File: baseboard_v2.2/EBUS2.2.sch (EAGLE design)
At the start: 51 parts, among them IC1 TLC393P, IC2 78L05Z

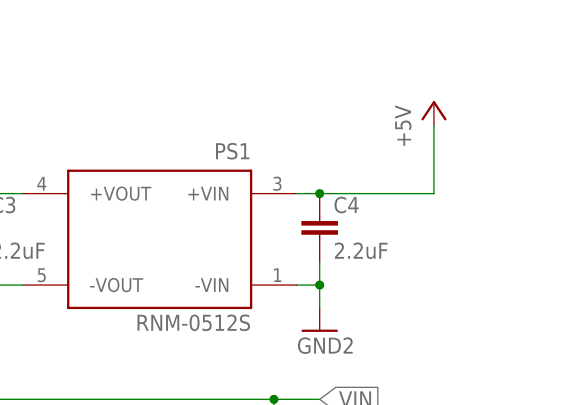
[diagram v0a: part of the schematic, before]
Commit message: change external power pinout
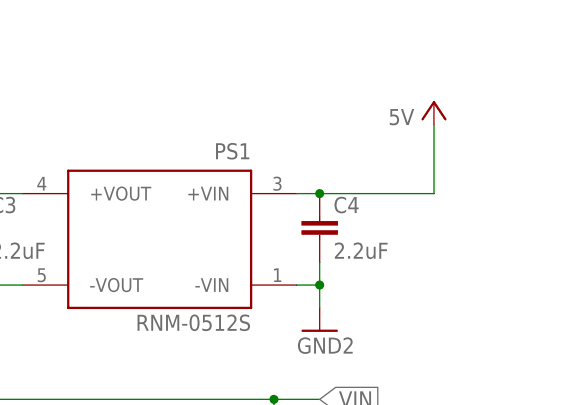
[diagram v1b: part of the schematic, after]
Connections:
- net +5V: no longer C4.1, PS1.+VIN
- net 5V: now also C4.1, PS1.+VIN
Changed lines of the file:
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@@
 <layer number="91" name="Nets" color="2" fill="1" visible="yes" active="yes"/>
 <layer number="92" name="Busses" color="1" fill="1" visible="yes" active="yes"/>
-<layer number="93" name="Pins" color="2" fill="1" visible="no" active="yes"/>
+<layer number="93" name="Pins" color="2" fill="1" visible="yes" active="yes"/>
 <layer number="94" name="Symbols" color="4" fill="1" visible="yes" active="yes"/>
 <layer number="95" name="Names" color="7" fill="1" visible="yes" active="yes"/>
@@
 <attribute name="VALUE" x="291.084" y="180.721" size="1.778" layer="96" font="vector"/>
 </instance>
-<instance part="P+7" gate="1" x="302.26" y="198.12" smashed="yes">
-<attribute name="VALUE" x="299.72" y="193.04" size="1.778" layer="96" rot="R90"/>
-</instance>
+<instance part="P+7" gate="1" x="302.26" y="198.12" smashed="yes"/>
 <instance part="GND15" gate="1" x="289.56" y="172.72" smashed="yes">
 <attribute name="VALUE" x="287.02" y="170.18" size="1.778" layer="96"/>
@@
 <wire x1="76.2" y1="71.12" x2="88.9" y2="71.12" width="0.1524" layer="91"/>
 <label x="88.9" y="71.12" size="1.778" layer="95" xref="yes"/>
+</segment>
+<segment>
+<pinref part="P+7" gate="1" pin="+5V"/>
+<wire x1="302.26" y1="195.58" x2="302.26" y2="187.96" width="0.1524" layer="91"/>
+<pinref part="PS1" gate="G$1" pin="+VIN"/>
+<pinref part="C4" gate="G$1" pin="1"/>
+<wire x1="287.02" y1="187.96" x2="289.56" y2="187.96" width="0.1524" layer="91"/>
+<wire x1="302.26" y1="187.96" x2="289.56" y2="187.96" width="0.1524" layer="91"/>
+<junction x="289.56" y="187.96"/>
+<label x="297.18" y="195.58" size="1.778" layer="95"/>
 </segment>
 </net>
@@
 </segment>
 <segment>
-<pinref part="P+7" gate="1" pin="+5V"/>
-<wire x1="302.26" y1="195.58" x2="302.26" y2="187.96" width="0.1524" layer="91"/>
-<pinref part="PS1" gate="G$1" pin="+VIN"/>
-<pinref part="C4" gate="G$1" pin="1"/>
-<wire x1="287.02" y1="187.96" x2="289.56" y2="187.96" width="0.1524" layer="91"/>
-<wire x1="302.26" y1="187.96" x2="289.56" y2="187.96" width="0.1524" layer="91"/>
-<junction x="289.56" y="187.96"/>
-</segment>
-<segment>

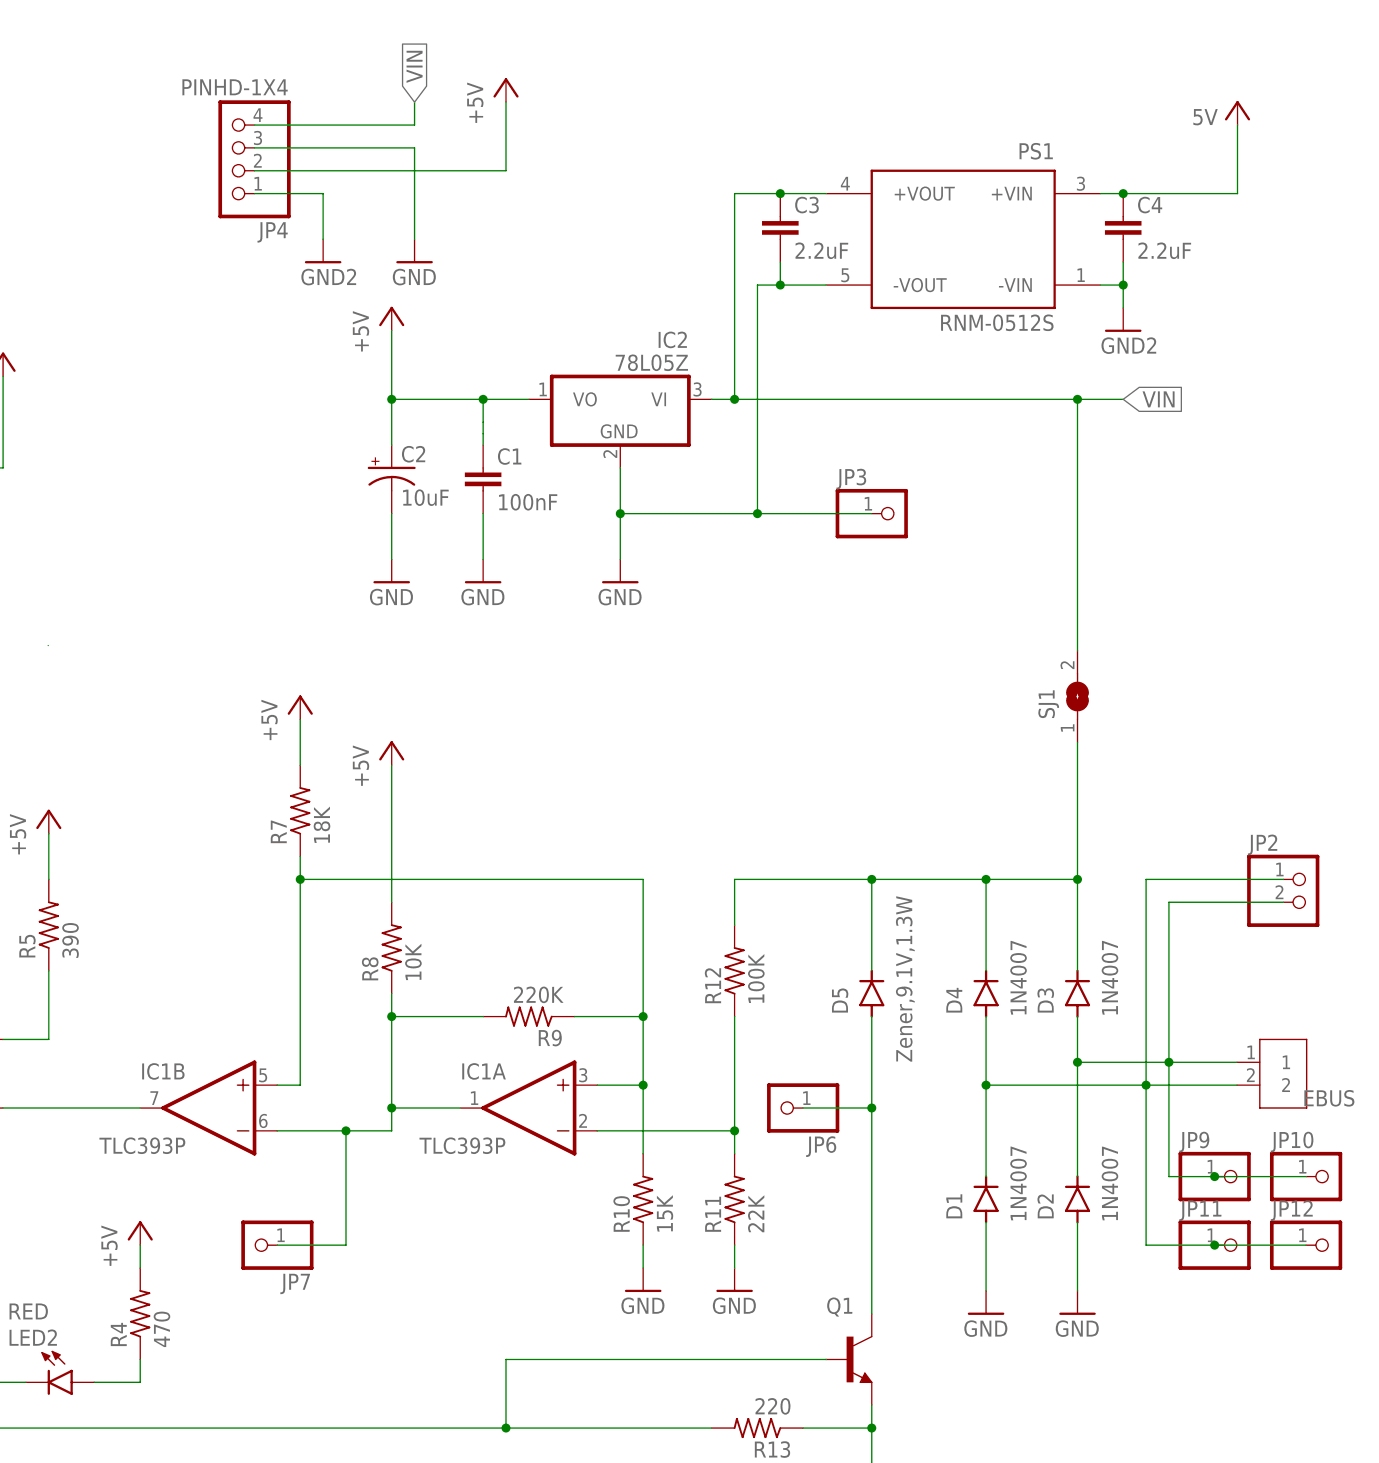
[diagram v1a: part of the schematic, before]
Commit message: Fix TLC389P powering
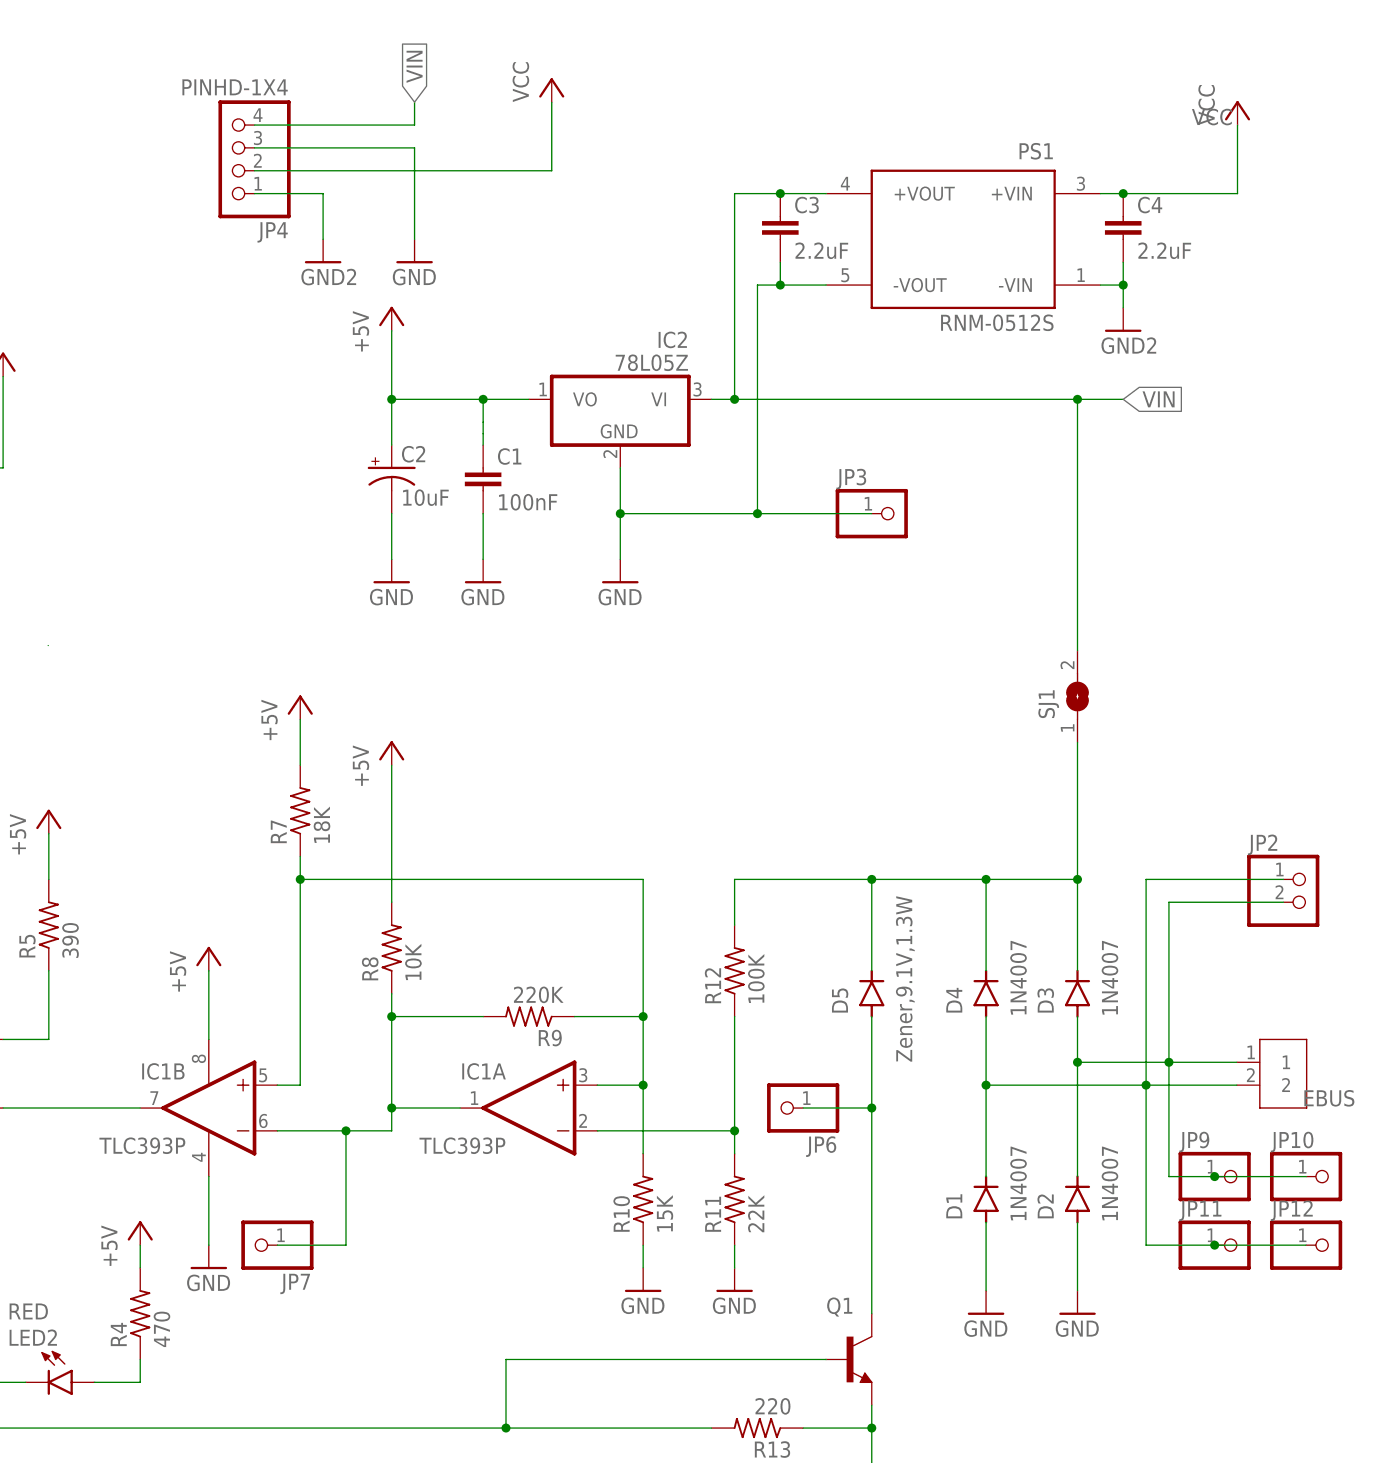
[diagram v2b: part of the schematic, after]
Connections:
- new net VCC: C4.1, JP4.2, PS1.+VIN
- net +5V: now also IC1P.V+; no longer JP4.2
- net 5V: no longer C4.1, PS1.+VIN
- net GND: now also IC1P.V-
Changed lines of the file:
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@@
 <part name="PS1" library="RNM-0512S" deviceset="RNM-0512S" device=""/>
 <part name="C4" library="SparkFun-Capacitors" library_urn="urn:adsk.eagle:library:510" deviceset="0.1UF" device="-KIT-EZ-50V-20%" package3d_urn="urn:adsk.eagle:package:37428/1" value="2.2uF"/>
-<part name="P+7" library="supply1" library_urn="urn:adsk.eagle:library:371" deviceset="+5V" device=""/>
 <part name="GND15" library="supply1" library_urn="urn:adsk.eagle:library:371" deviceset="GND" device="" value="GND2"/>
 <part name="JP4" library="Connector" library_urn="urn:adsk.eagle:library:16378166" deviceset="PINHD-1X4" device="" package3d_urn="urn:adsk.eagle:package:22407/2"/>
 <part name="GND16" library="supply1" library_urn="urn:adsk.eagle:library:371" deviceset="GND" device="" value="GND2"/>
+<part name="GND17" library="supply1" library_urn="urn:adsk.eagle:library:371" deviceset="GND" device="" value="GND"/>
+<part name="P+9" library="supply1" library_urn="urn:adsk.eagle:library:371" deviceset="VCC" device=""/>
+<part name="P+7" library="supply1" library_urn="urn:adsk.eagle:library:371" deviceset="VCC" device=""/>
 <part name="P+8" library="supply1" library_urn="urn:adsk.eagle:library:371" deviceset="+5V" device=""/>
-<part name="GND17" library="supply1" library_urn="urn:adsk.eagle:library:371" deviceset="GND" device="" value="GND"/>
+<part name="GND18" library="supply1" library_urn="urn:adsk.eagle:library:371" deviceset="GND" device="" value="GND"/>
 </parts>
 <sheets>
@@
 <attribute name="VALUE" x="291.084" y="180.721" size="1.778" layer="96" font="vector"/>
 </instance>
-<instance part="P+7" gate="1" x="302.26" y="198.12" smashed="yes"/>
 <instance part="GND15" gate="1" x="289.56" y="172.72" smashed="yes">
 <attribute name="VALUE" x="287.02" y="170.18" size="1.778" layer="96"/>
@@
 <attribute name="VALUE" x="198.12" y="177.8" size="1.778" layer="96"/>
 </instance>
-<instance part="P+8" gate="1" x="220.98" y="200.66" smashed="yes">
-<attribute name="VALUE" x="218.44" y="195.58" size="1.778" layer="96" rot="R90"/>
-</instance>
 <instance part="GND17" gate="1" x="210.82" y="180.34" smashed="yes">
 <attribute name="VALUE" x="208.28" y="177.8" size="1.778" layer="96"/>
+</instance>
+<instance part="P+9" gate="VCC" x="226.06" y="200.66" smashed="yes">
+<attribute name="VALUE" x="223.52" y="198.12" size="1.778" layer="96" rot="R90"/>
+</instance>
+<instance part="P+7" gate="VCC" x="302.26" y="198.12" smashed="yes">
+<attribute name="VALUE" x="299.72" y="195.58" size="1.778" layer="96" rot="R90"/>
+</instance>
+<instance part="IC1" gate="P" x="187.96" y="86.36" smashed="yes"/>
+<instance part="P+8" gate="1" x="187.96" y="104.14" smashed="yes">
+<attribute name="VALUE" x="185.42" y="99.06" size="1.778" layer="96" rot="R90"/>
+</instance>
+<instance part="GND18" gate="1" x="187.96" y="68.58" smashed="yes">
+<attribute name="VALUE" x="185.42" y="66.04" size="1.778" layer="96"/>
 </instance>
 </instances>
@@
 <wire x1="210.82" y1="193.04" x2="210.82" y2="182.88" width="0.1524" layer="91"/>
 </segment>
+<segment>
+<pinref part="IC1" gate="P" pin="V-"/>
+<pinref part="GND18" gate="1" pin="GND"/>
+<wire x1="187.96" y1="71.12" x2="187.96" y2="78.74" width="0.1524" layer="91"/>
+</segment>
 </net>
 <net name="5V" class="0">
@@
 <wire x1="76.2" y1="71.12" x2="88.9" y2="71.12" width="0.1524" layer="91"/>
 <label x="88.9" y="71.12" size="1.778" layer="95" xref="yes"/>
-</segment>
-<segment>
-<pinref part="P+7" gate="1" pin="+5V"/>
-<wire x1="302.26" y1="195.58" x2="302.26" y2="187.96" width="0.1524" layer="91"/>
-<pinref part="PS1" gate="G$1" pin="+VIN"/>
-<pinref part="C4" gate="G$1" pin="1"/>
-<wire x1="287.02" y1="187.96" x2="289.56" y2="187.96" width="0.1524" layer="91"/>
-<wire x1="302.26" y1="187.96" x2="289.56" y2="187.96" width="0.1524" layer="91"/>
-<junction x="289.56" y="187.96"/>
-<label x="297.18" y="195.58" size="1.778" layer="95"/>
 </segment>
 </net>
@@
 </segment>
 <segment>
+<pinref part="IC1" gate="P" pin="V+"/>
 <pinref part="P+8" gate="1" pin="+5V"/>
-<wire x1="220.98" y1="198.12" x2="220.98" y2="190.5" width="0.1524" layer="91"/>
-<pinref part="JP4" gate="A" pin="2"/>
-<wire x1="220.98" y1="190.5" x2="193.04" y2="190.5" width="0.1524" layer="91"/>
+<wire x1="187.96" y1="101.6" x2="187.96" y2="93.98" width="0.1524" layer="91"/>
 </segment>
 </net>
@@
 </segment>
 </net>
+<net name="VCC" class="0">
+<segment>
+<pinref part="JP4" gate="A" pin="2"/>
+<wire x1="193.04" y1="190.5" x2="226.06" y2="190.5" width="0.1524" layer="91"/>
+<pinref part="P+9" gate="VCC" pin="VCC"/>
+<wire x1="226.06" y1="190.5" x2="226.06" y2="198.12" width="0.1524" layer="91"/>
+</segment>
+<segment>
+<wire x1="302.26" y1="195.58" x2="302.26" y2="187.96" width="0.1524" layer="91"/>
+<pinref part="PS1" gate="G$1" pin="+VIN"/>
+<pinref part="C4" gate="G$1" pin="1"/>
+<wire x1="287.02" y1="187.96" x2="289.56" y2="187.96" width="0.1524" layer="91"/>
+<wire x1="302.26" y1="187.96" x2="289.56" y2="187.96" width="0.1524" layer="91"/>
+<junction x="289.56" y="187.96"/>
+<label x="297.18" y="195.58" size="1.778" layer="95"/>
+<pinref part="P+7" gate="VCC" pin="VCC"/>
+</segment>
+</net>
